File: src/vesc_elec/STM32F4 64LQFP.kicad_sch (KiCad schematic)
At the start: 18 parts, among them J7 Conn_02x03_Odd_Even, U5 STM32F405RGT6, Y1 Crystal_GND24_Small

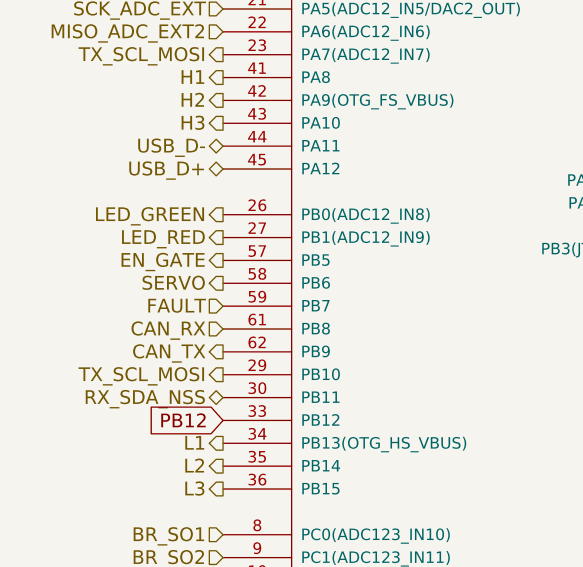
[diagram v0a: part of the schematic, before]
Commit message: Remove extra footprint libraries
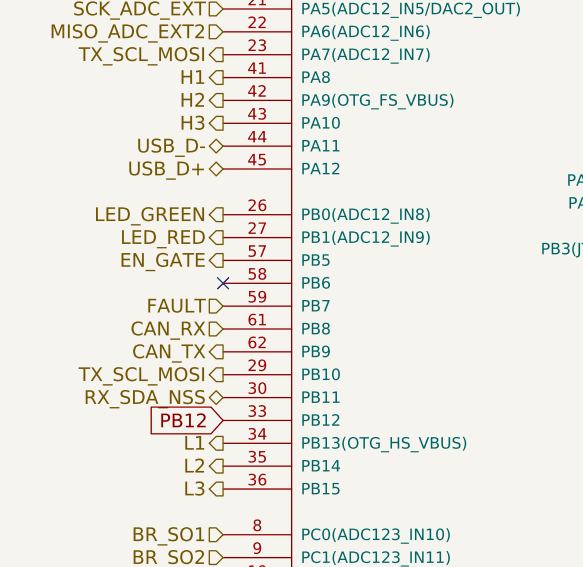
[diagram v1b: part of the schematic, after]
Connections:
- net SERVO: no longer names the net of U5.58 (PB6)
- no-connect marks 0 -> 1
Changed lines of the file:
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@@
 		(color 0 0 0 0)
 	)
+	(no_connect
+		(at 114.3 87.63)
+	)
 	(wire
 		(pts
@@
 		)
 	)
-	(hierarchical_label "SERVO"
-		(shape output)
-		(at 114.3 87.63 180)
-		(effects
-			(font
-				(size 1.524 1.524)
-			)
-			(justify right)
-		)
-	)

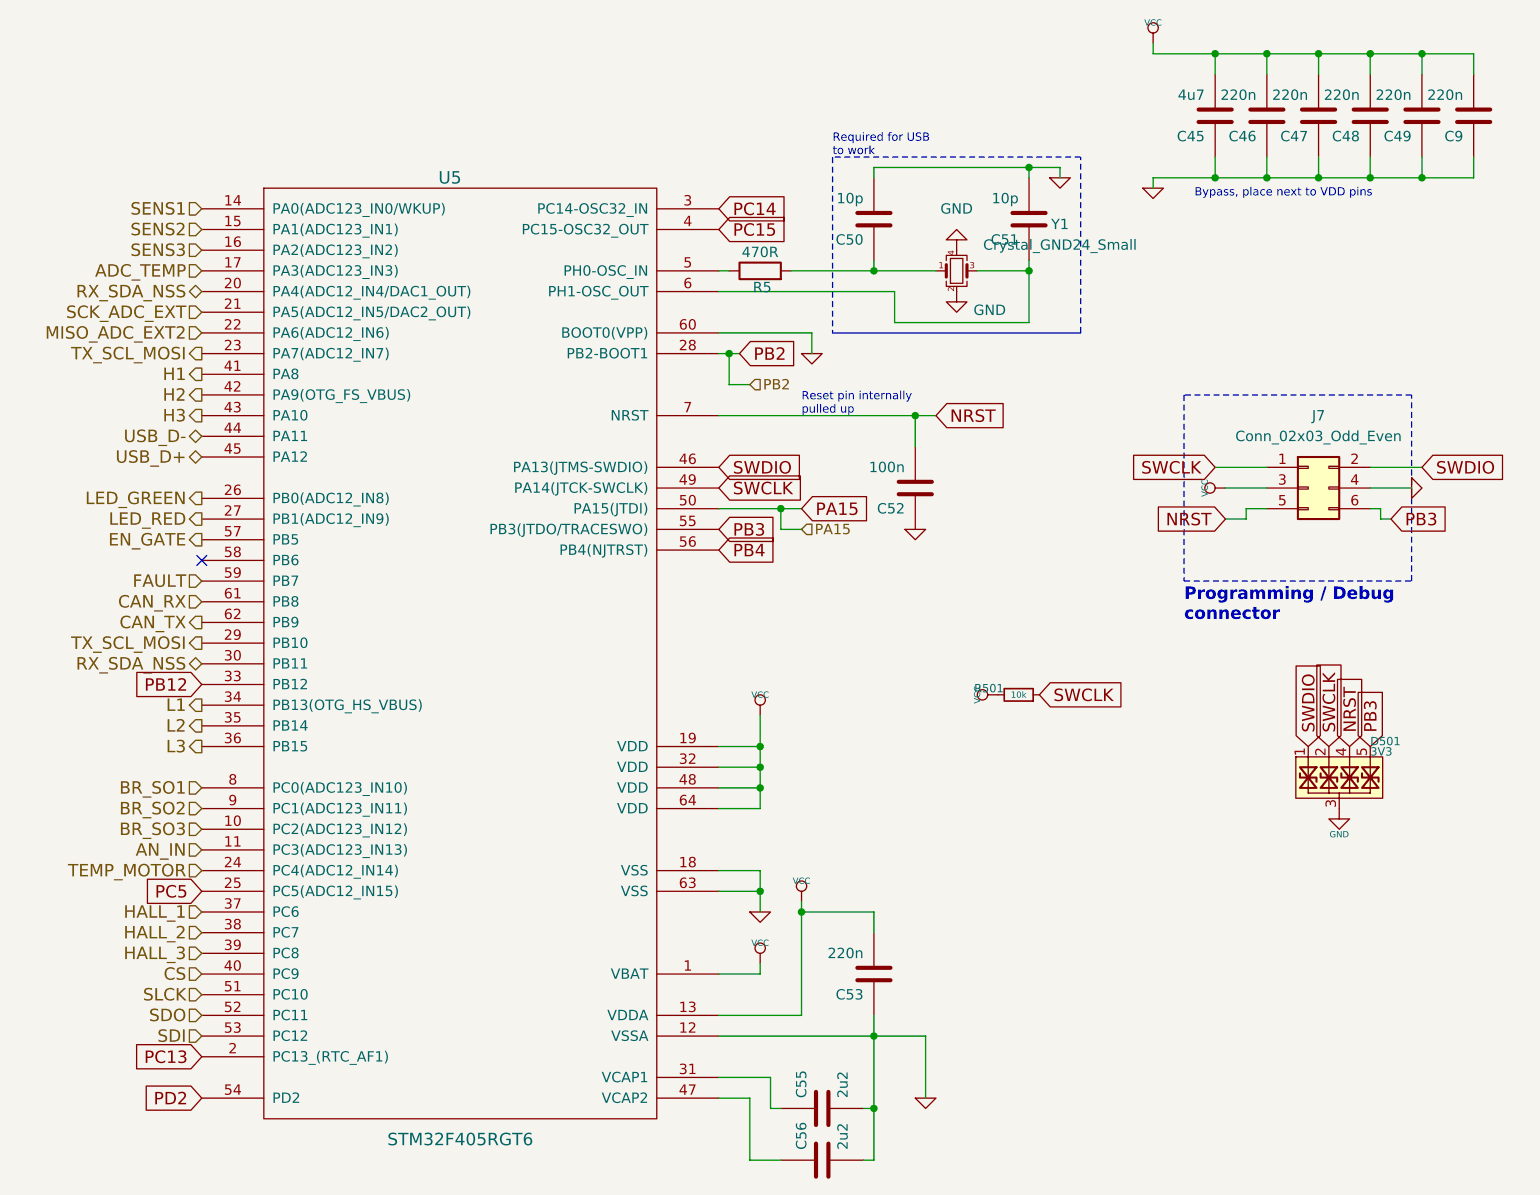
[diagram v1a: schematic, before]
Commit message: Remove unused pins on VESC schematic
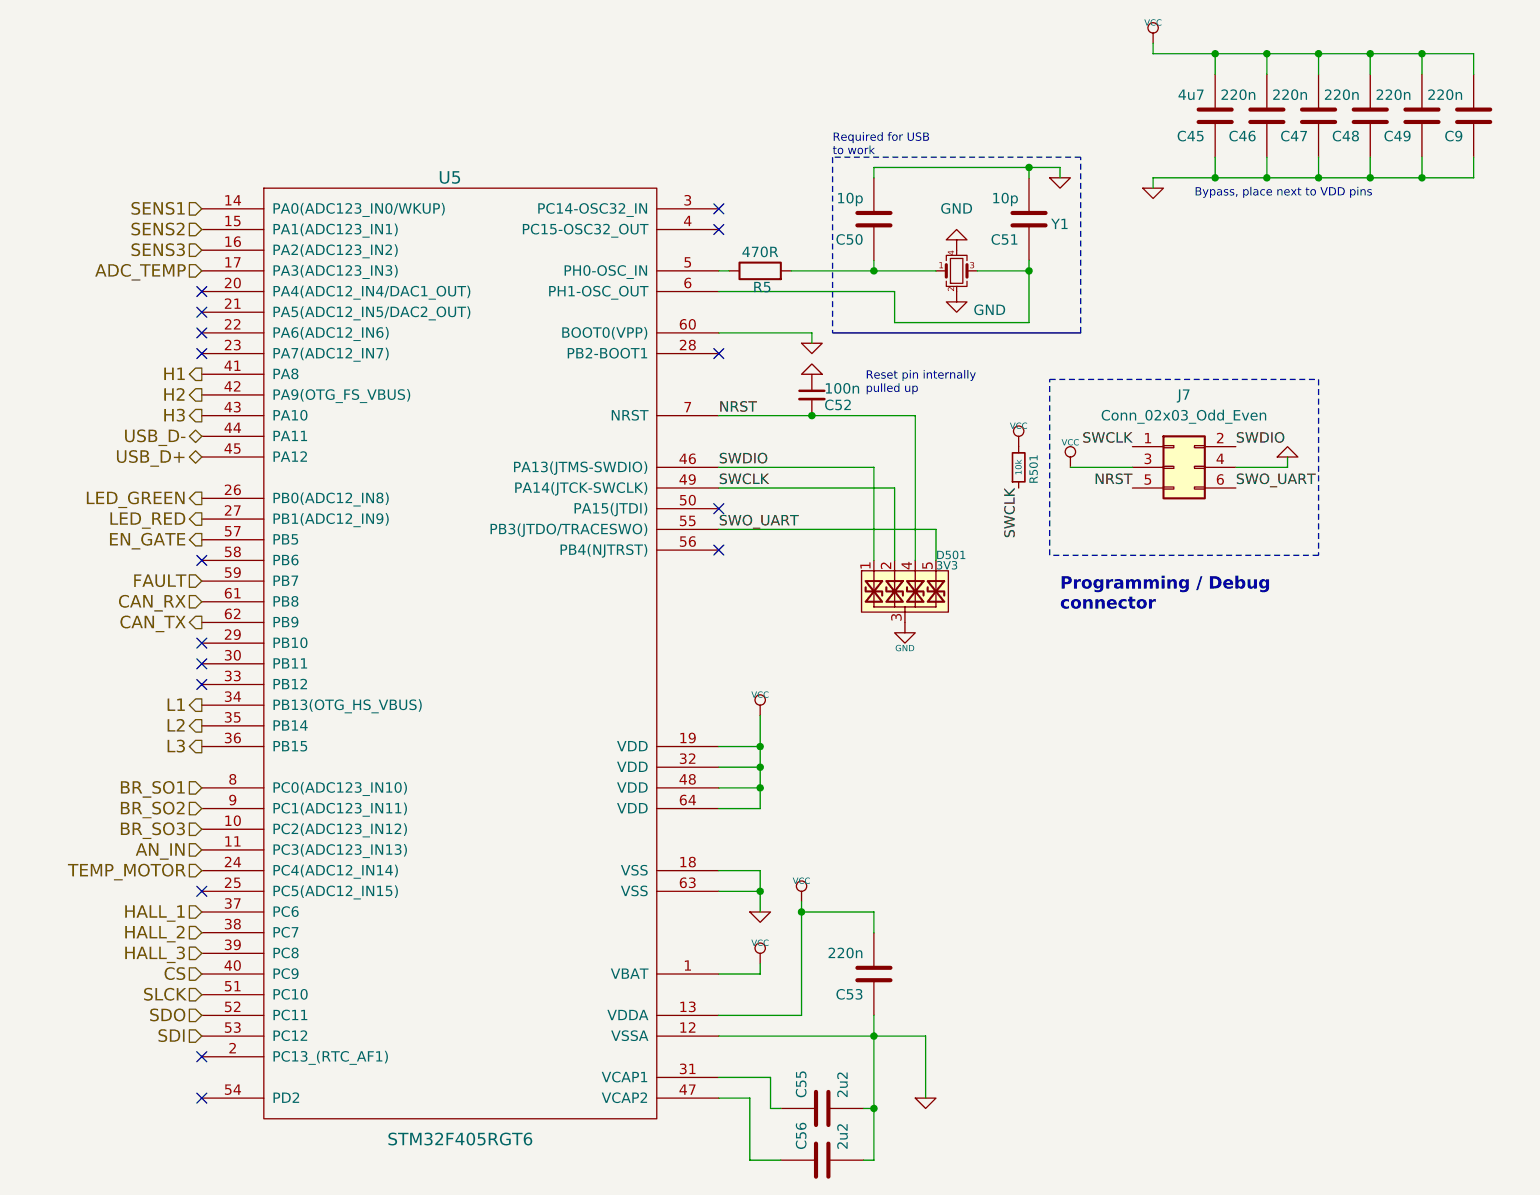
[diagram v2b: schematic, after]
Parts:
- C52: symbol BLDC_4-rescue:C-RESCUE-BLDC_4 -> Bluesat:C_CompactH
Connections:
- net MISO_ADC_EXT2: no longer names the net of U5.22 (PA6(ADC12_IN6))
- net PA15: no longer names the net of U5.50 (PA15(JTDI))
- net PB12: no longer names the net of U5.33 (PB12)
- net PB2: no longer names the net of U5.28 (PB2-BOOT1)
- net PB3 renamed SWO_UART
- net PB4: no longer names the net of U5.56 (PB4(NJTRST))
- net PC13: no longer names the net of U5.2 (PC13_(RTC_AF1))
- net PC14: no longer names the net of U5.3 (PC14-OSC32_IN)
- net PC15: no longer names the net of U5.4 (PC15-OSC32_OUT)
- net PC5: no longer names the net of U5.25 (PC5(ADC12_IN15))
- net PD2: no longer names the net of U5.54 (PD2)
- net RX_SDA_NSS: no longer names the net of U5.20 (PA4(ADC12_IN4/DAC1_OUT))
- net RX_SDA_NSS: no longer U5.30 (PB11)
- net SCK_ADC_EXT: no longer names the net of U5.21 (PA5(ADC12_IN5/DAC2_OUT))
- net TX_SCL_MOSI: no longer names the net of U5.23 (PA7(ADC12_IN7))
- net TX_SCL_MOSI: no longer U5.29 (PB10)
- no-connect marks 1 -> 16
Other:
- moved on the sheet: C52, D501, J7, R501

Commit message: Fix rotated IDC6 on CPM/MPM/VESC/Stepper/USB Hub (#120)
* Fix rotated IDC6 on CPM/MPM/VESC/Stepper/USB Hub

* Fix VESC
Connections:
- net GND: now also J7.3 (Pin_3); no longer J7.4 (Pin_4)
- net NRST: now also J7.2 (Pin_2); no longer J7.5 (Pin_5)
- net SWCLK: now also J7.6 (Pin_6); no longer J7.1 (Pin_1)
- net SWDIO: now also J7.5 (Pin_5); no longer J7.2 (Pin_2)
- net SWO_UART: now also J7.1 (Pin_1); no longer J7.6 (Pin_6)
- net VCC: now also J7.4 (Pin_4); no longer J7.3 (Pin_3)
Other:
- moved on the sheet: J7
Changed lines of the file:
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@@
 	(symbol
 		(lib_id "Connector_Generic:Conn_02x03_Odd_Even")
-		(at 233.68 76.2 0)
+		(at 236.22 76.2 180)
 		(unit 1)
 		(exclude_from_sim no)
@@
 		(dnp no)
 		(property "Reference" "J7"
-			(at 234.95 67.31 0)
+			(at 234.95 85.09 0)
 			(effects
 				(font
@@
 		)
 		(property "Value" "Conn_02x03_Odd_Even"
-			(at 234.95 69.85 0)
+			(at 234.95 82.55 0)
 			(effects
 				(font
@@
 		)
 		(property "Footprint" "Bluesat:IDC6"
-			(at 233.68 76.2 0)
+			(at 236.22 76.2 0)
 			(effects
 				(font
@@
 		)
 		(property "Datasheet" "~"
-			(at 233.68 76.2 0)
+			(at 236.22 76.2 0)
 			(effects
 				(font
@@
 		)
 		(property "Description" "Generic connector, double row, 02x03, odd/even pin numbering scheme (row 1 odd numbers, row 2 even numbers), script generated (kicad-library-utils/schlib/autogen/connector/)"
-			(at 233.68 76.2 0)
+			(at 236.22 76.2 0)
 			(effects
 				(font
